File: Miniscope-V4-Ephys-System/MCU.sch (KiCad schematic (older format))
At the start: 37 parts, among them J14 Conn_01x05, J15 Conn_01x01, J16 Conn_01x01, J17 Conn_01x01, J18 Conn_01x01, J19 Conn_01x01, J20 Conn_01x01, J21 Conn_01x01, J22 Conn_01x01, Q1 MMBT3904LP-7B, U4 ATSAME70N21A-CN, U5 MCP1711T-18I/5X, Y1 SMD_CRYSTAL

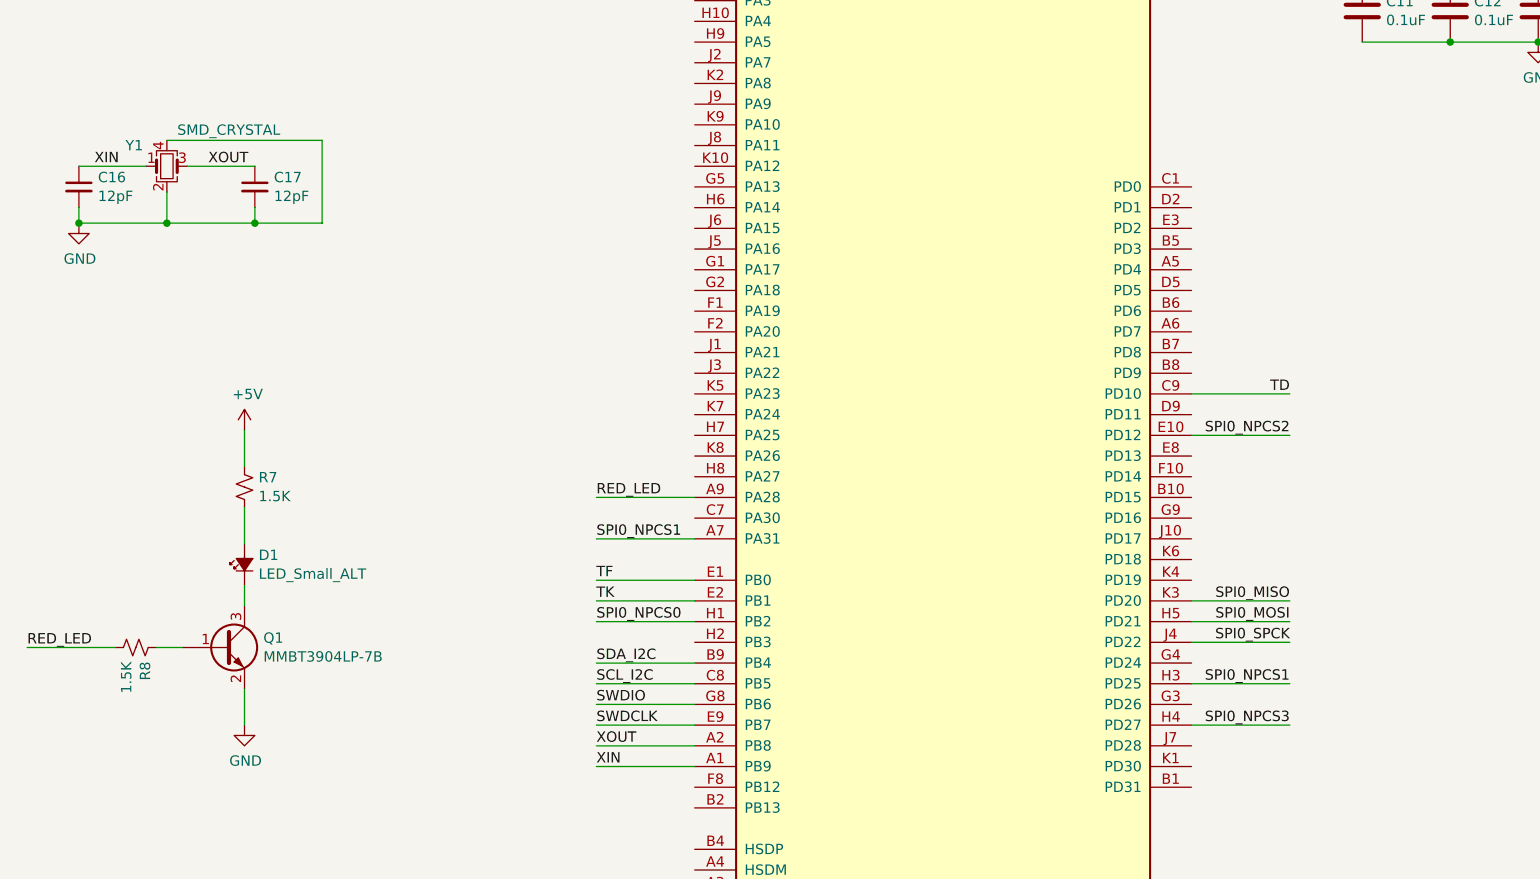
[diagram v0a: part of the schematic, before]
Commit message: Finish layout of MCU PCB and routing of almost all traces.
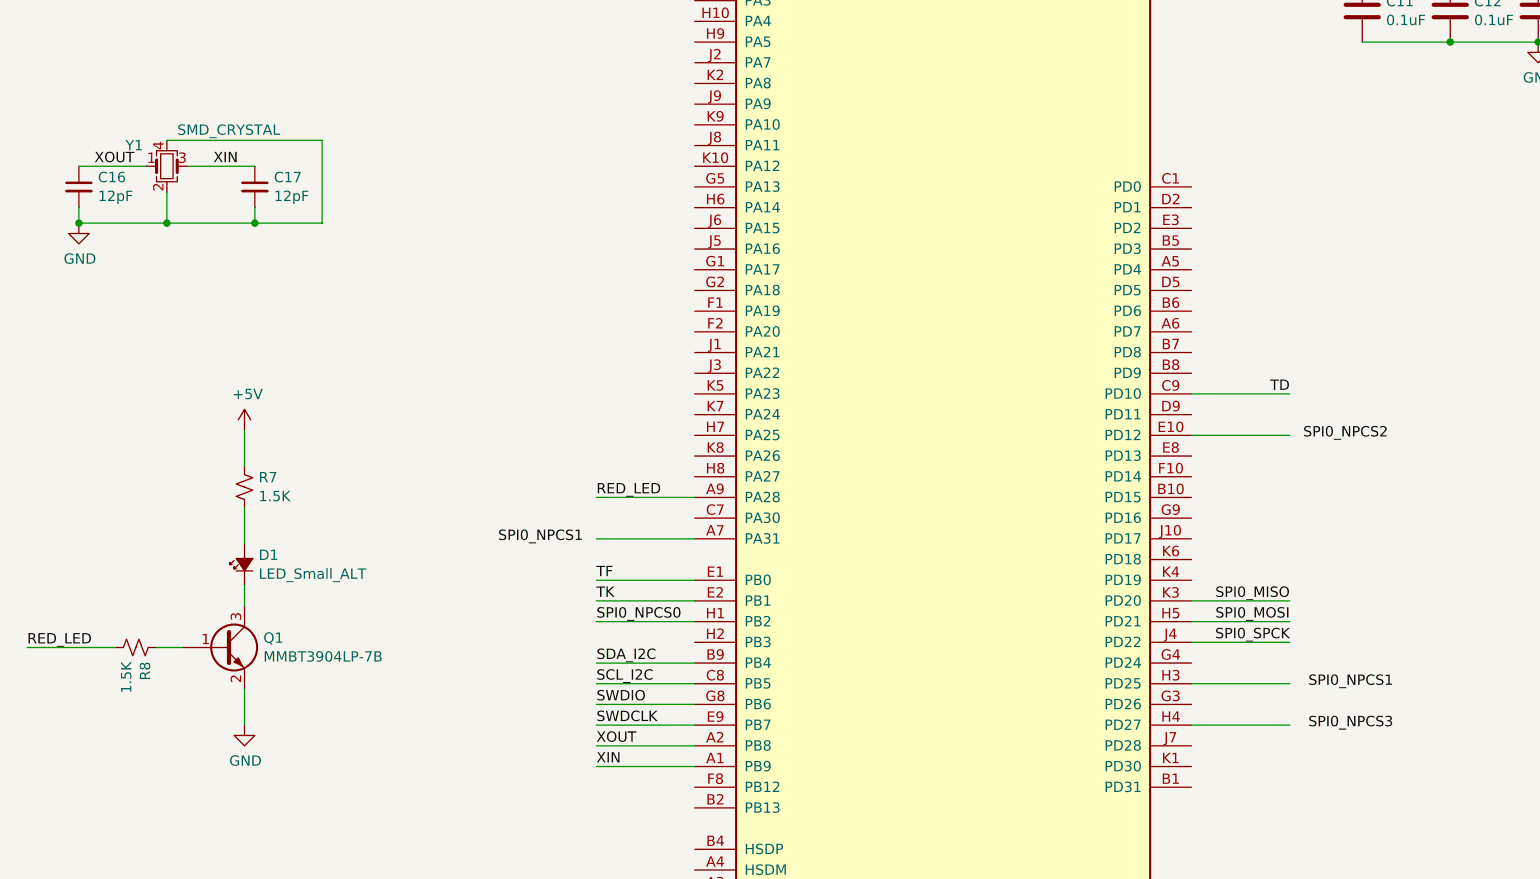
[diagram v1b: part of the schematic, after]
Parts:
- J15, J16: footprint TestPoint:TestPoint_Pad_1.0x1.0mm -> .Connector:Conn_1x1_250x750_Pad
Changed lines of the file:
@@
 F 0 "J16" H 10405 5146 50  0000 L CNN
 F 1 "Conn_01x01" H 10405 5146 50  0001 L CNN
-F 2 "TestPoint:TestPoint_Pad_1.0x1.0mm" H 10405 5101 50  0001 L CNN
+F 2 ".Connector:Conn_1x1_250x750_Pad" H 10405 5101 50  0001 L CNN
 F 3 "~" H 10325 5150 50  0001 C CNN
 	1    10325 5150
@@
 F 0 "J15" H 10405 5046 50  0000 L CNN
 F 1 "Conn_01x01" H 10405 5046 50  0001 L CNN
-F 2 "TestPoint:TestPoint_Pad_1.0x1.0mm" H 10325 5050 50  0001 C CNN
+F 2 ".Connector:Conn_1x1_250x750_Pad" H 10325 5050 50  0001 C CNN
 F 3 "~" H 10325 5050 50  0001 C CNN
 	1    10325 5050
@@
 Text Label 3650 4275 0    50   ~ 0
 RED_LED
-Text Label 3650 4475 0    50   ~ 0
+Text Label 3175 4500 0    50   ~ 0
 SPI0_NPCS1
 Wire Wire Line
@@
 Text Label 7000 3775 2    50   ~ 0
 TD
-Text Label 7000 3975 2    50   ~ 0
+Text Label 7475 4000 2    50   ~ 0
 SPI0_NPCS2
 Text Label 7000 4775 2    50   ~ 0
@@
 Wire Wire Line
 	7000 5375 6525 5375
-Text Label 7000 5175 2    50   ~ 0
+Text Label 7500 5200 2    50   ~ 0
 SPI0_NPCS1
-Text Label 7000 5375 2    50   ~ 0
+Text Label 7500 5400 2    50   ~ 0
 SPI0_NPCS3
 $Comp
@@
 	1    0    0    -1
 $EndComp
-Text Label 1775 2675 0    50   ~ 0
+Text Label 1225 2675 0    50   ~ 0
 XOUT
-Text Label 1225 2675 0    50   ~ 0
+Text Label 1800 2675 0    50   ~ 0
 XIN
 $EndSCHEMATC

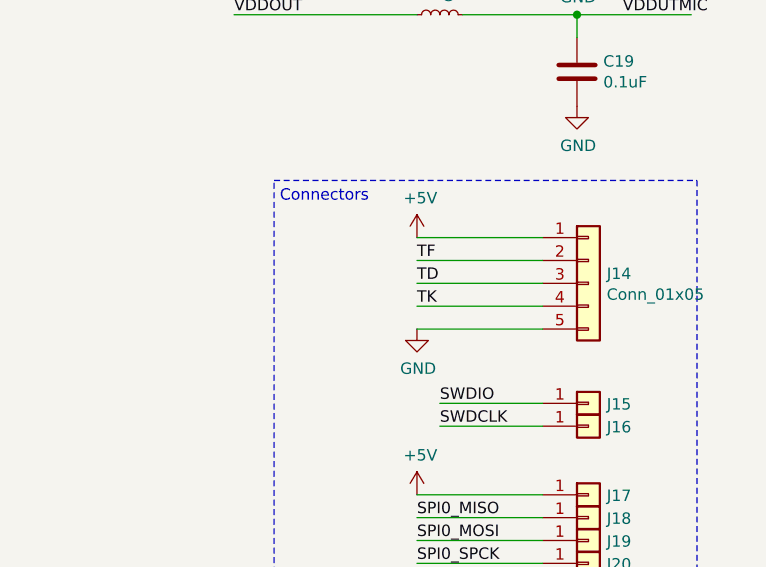
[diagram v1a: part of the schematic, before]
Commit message: Finish routing of all PCBs. Need to double check before fabrication.
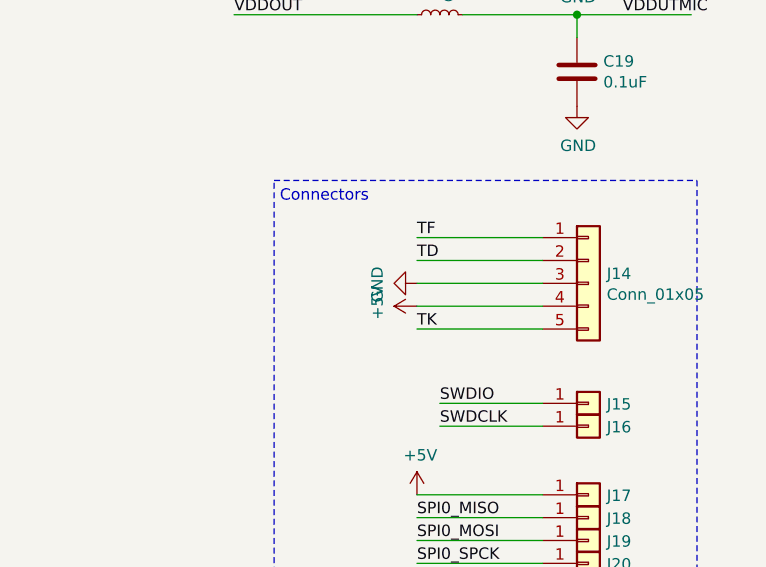
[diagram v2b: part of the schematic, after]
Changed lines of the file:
@@
 L power:GND #PWR0117
 U 1 1 5EEBC0D4
-P 9575 4725
-F 0 "#PWR0117" H 9575 4475 50  0001 C CNN
-F 1 "GND" H 9580 4552 50  0000 C CNN
-F 2 "" H 9575 4725 50  0001 C CNN
-F 3 "" H 9575 4725 50  0001 C CNN
-	1    9575 4725
-	1    0    0    -1
-$EndComp
-Text Label 9575 4625 0    50   ~ 0
+P 9575 4525
+F 0 "#PWR0117" H 9575 4275 50  0001 C CNN
+F 1 "GND" H 9580 4352 50  0000 C CNN
+F 2 "" H 9575 4525 50  0001 C CNN
+F 3 "" H 9575 4525 50  0001 C CNN
+	1    9575 4525
+	0    1    1    0
+$EndComp
+Text Label 9575 4725 0    50   ~ 0
 TK
-Text Label 9575 4525 0    50   ~ 0
+Text Label 9575 4425 0    50   ~ 0
 TD
-Text Label 9575 4425 0    50   ~ 0
+Text Label 9575 4325 0    50   ~ 0
 TF
 Wire Wire Line
@@
 L power:+5V #PWR0122
 U 1 1 5EEBC1FE
-P 9575 4325
-F 0 "#PWR0122" H 9575 4175 50  0001 C CNN
-F 1 "+5V" H 9590 4498 50  0000 C CNN
-F 2 "" H 9575 4325 50  0001 C CNN
-F 3 "" H 9575 4325 50  0001 C CNN
-	1    9575 4325
-	1    0    0    -1
-$EndComp
-$Comp
+P 9575 4625
+F 0 "#PWR0122" H 9575 4475 50  0001 C CNN
+F 1 "+5V" H 9590 4798 50  0000 C CNN
+F 2 "" H 9575 4625 50  0001 C CNN
+F 3 "" H 9575 4625 50  0001 C CNN
+	1    9575 4625
+	0    -1   -1   0
+$EndComp
+$Comp

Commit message: Switch spring connectors to a lower profile option
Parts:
- J17, J18, J19, J20, J21, J22: footprint .Connector:Spring_2306654_3 -> .Connector:Spring_2306334
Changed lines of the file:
@@
 F 0 "J17" H 10405 5446 50  0000 L CNN
 F 1 "Conn_01x01" H 10405 5446 50  0001 L CNN
-F 2 ".Connector:Spring_2306654_3" H 10325 5450 50  0001 C CNN
+F 2 ".Connector:Spring_2306334" H 10325 5450 50  0001 C CNN
 F 3 "~" H 10325 5450 50  0001 C CNN
 	1    10325 5450
@@
 F 0 "J18" H 10405 5546 50  0000 L CNN
 F 1 "Conn_01x01" H 10405 5546 50  0001 L CNN
-F 2 ".Connector:Spring_2306654_3" H 10325 5550 50  0001 C CNN
+F 2 ".Connector:Spring_2306334" H 10325 5550 50  0001 C CNN
 F 3 "~" H 10325 5550 50  0001 C CNN
 	1    10325 5550
@@
 F 0 "J19" H 10405 5646 50  0000 L CNN
 F 1 "Conn_01x01" H 10405 5646 50  0001 L CNN
-F 2 ".Connector:Spring_2306654_3" H 10325 5650 50  0001 C CNN
+F 2 ".Connector:Spring_2306334" H 10325 5650 50  0001 C CNN
 F 3 "~" H 10325 5650 50  0001 C CNN
 	1    10325 5650
@@
 F 0 "J20" H 10405 5746 50  0000 L CNN
 F 1 "Conn_01x01" H 10405 5746 50  0001 L CNN
-F 2 ".Connector:Spring_2306654_3" H 10325 5750 50  0001 C CNN
+F 2 ".Connector:Spring_2306334" H 10325 5750 50  0001 C CNN
 F 3 "~" H 10325 5750 50  0001 C CNN
 	1    10325 5750
@@
 F 0 "J21" H 10405 5846 50  0000 L CNN
 F 1 "Conn_01x01" H 10405 5846 50  0001 L CNN
-F 2 ".Connector:Spring_2306654_3" H 10325 5850 50  0001 C CNN
+F 2 ".Connector:Spring_2306334" H 10325 5850 50  0001 C CNN
 F 3 "~" H 10325 5850 50  0001 C CNN
 	1    10325 5850
@@
 F 0 "J22" H 10405 5946 50  0000 L CNN
 F 1 "Conn_01x01" H 10405 5946 50  0001 L CNN
-F 2 ".Connector:Spring_2306654_3" H 10325 5950 50  0001 C CNN
+F 2 ".Connector:Spring_2306334" H 10325 5950 50  0001 C CNN
 F 3 "~" H 10325 5950 50  0001 C CNN
 	1    10325 5950
